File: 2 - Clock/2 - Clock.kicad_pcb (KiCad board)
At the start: 2 copper layers, 100 x 100 mm, 79 parts, among them J1 BUS 1, J2 RST/CLK TP, SW1 RESET, SW2 MODE, SW3 SPEED, SW4 STEP, SW5 BOOT SPEED, SW6 BOOT MODE, SW7 RESET FAST LSB, SW8 RESET FAST MSB, U1 74AC14, U10 74AC112, U11 74AC74, U12 LMC555, U13 74AC74, U14 74HC251, U15 74HC138, U16 74HC251, U17 74HC251, U2 74AC174, U3 74AC08, U4 74AC14, U5 74AC74, U6 74AC74, U7 74AC74, U8 74AC74, U9 74AC112, X1 14.7456MHz

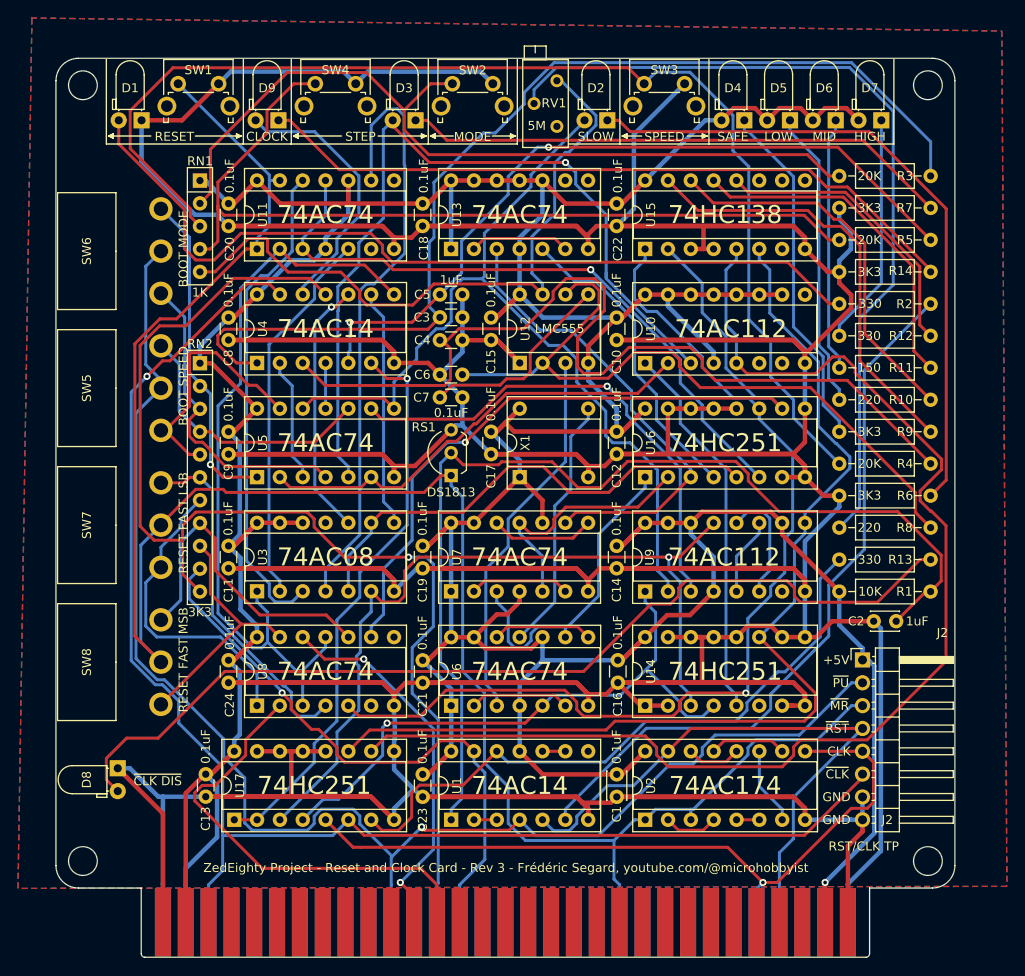
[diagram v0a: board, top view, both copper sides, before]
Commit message: Clock card updated
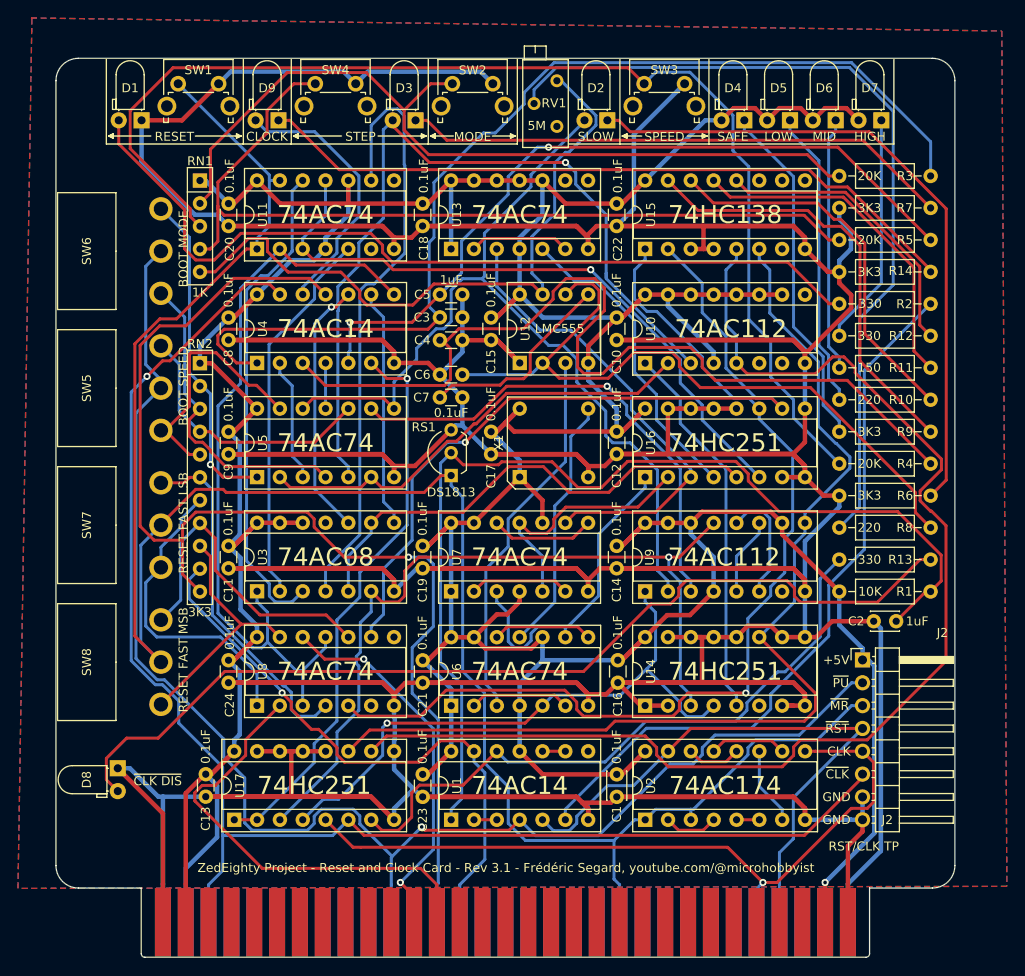
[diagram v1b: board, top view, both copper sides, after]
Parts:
- J1: footprint 0 - Library:BUS_XT -> 0_Library:BUS_XT_Proto
- SW5, SW6, SW7, SW8: footprint 0 - Library:Microswitch_4.7mm_spacing -> 0_Library:Microswitch_4.7mm_spacing
- X1: footprint 0 - Library:DIP-8-4_W7.62mm_Oscillator_Socket -> 0_Library:DIP-8-4_W7.62mm_Oscillator_Socket
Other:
- outline, holes or cut-outs redrawn
- rule pad_to_mask_clearance: 0.2 -> 0
- board text added: "ZedEighty Project - Reset and Clock Card - Rev 3.1 - Frédéric Segard, youtube.com/@microhobbyist"
- board text removed: "ZedEighty Project - Reset and Clock Card - Rev 3 - Frédéric Segard, youtube.com/@microhobbyist"
